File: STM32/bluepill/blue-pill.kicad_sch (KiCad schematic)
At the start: 36 parts, among them J1 USB_B_Micro, J2 J-Link, J3 BOOTx, J4 P3 Header, J5 P4 Header, SW1 RST, U1 RT9193, U2 STM32F103C8T6, Y1 8MHz, Y2 32.768k

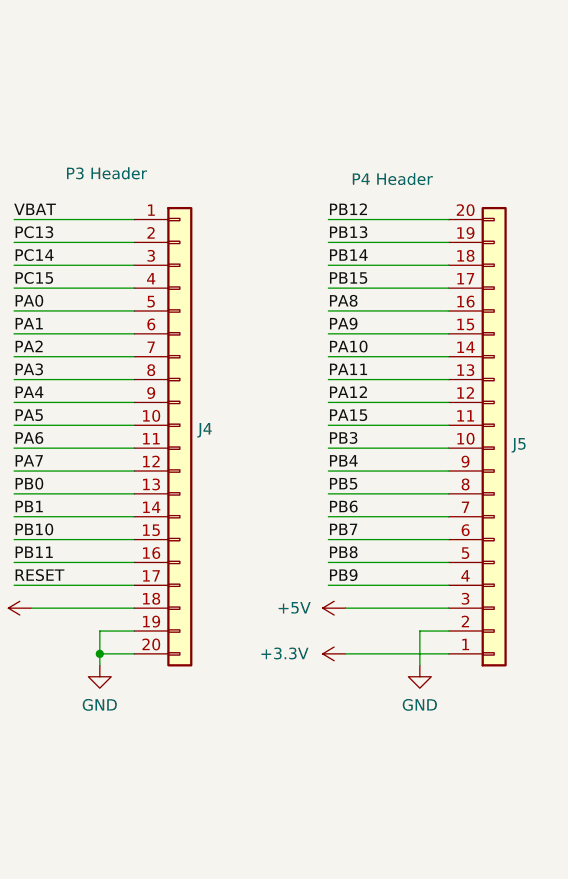
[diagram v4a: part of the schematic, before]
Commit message: Fix confusing P4 orientation
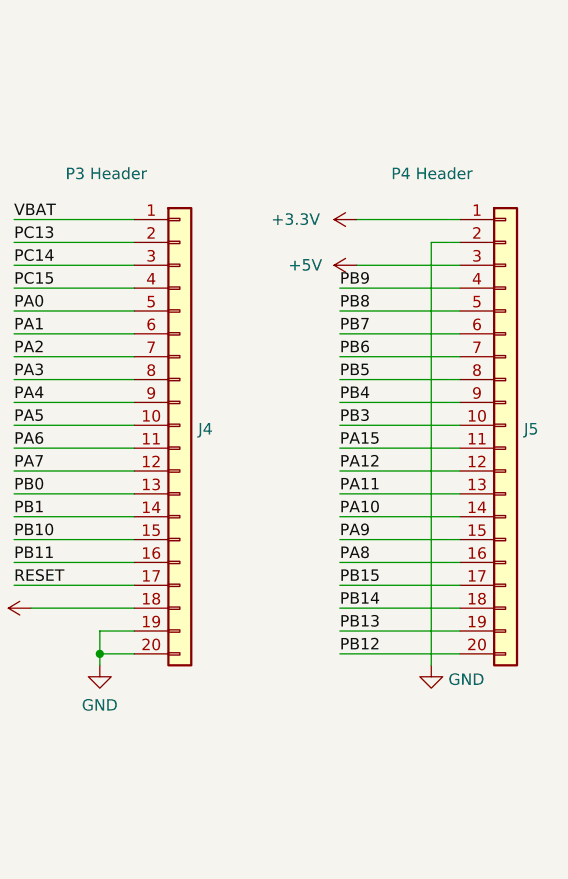
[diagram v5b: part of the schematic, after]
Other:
- moved on the sheet: J5

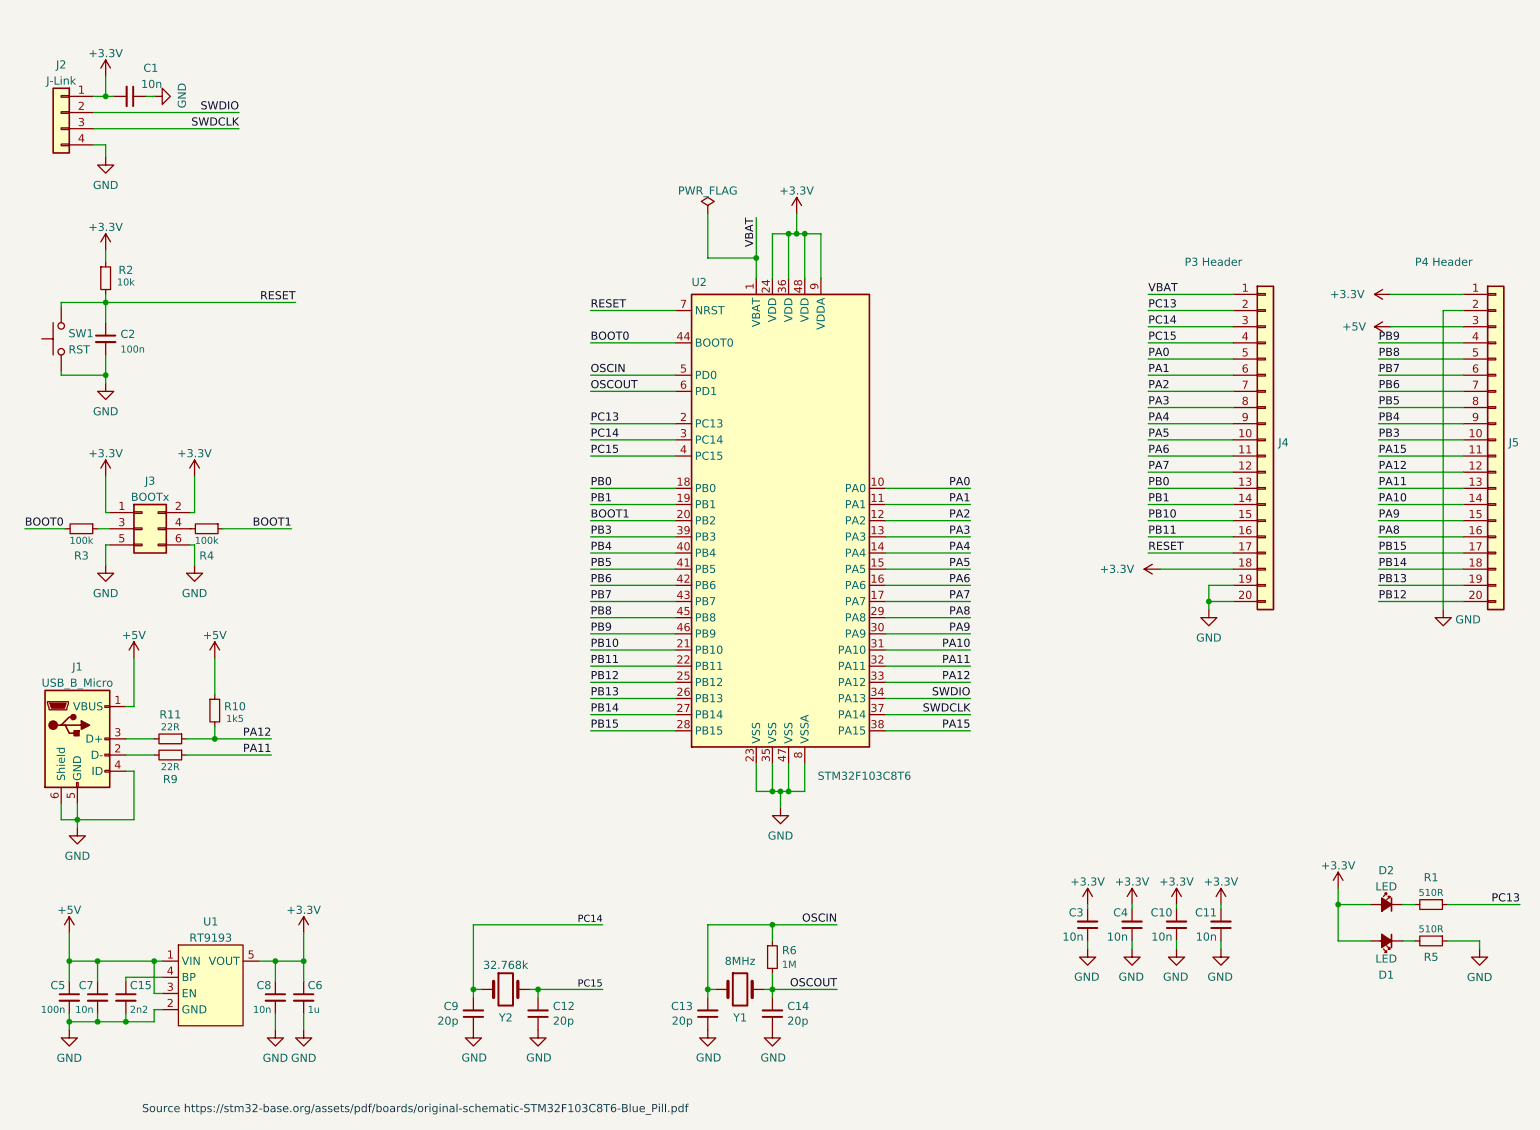
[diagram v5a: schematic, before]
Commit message: Fix grid alignment and update to KiCad 9
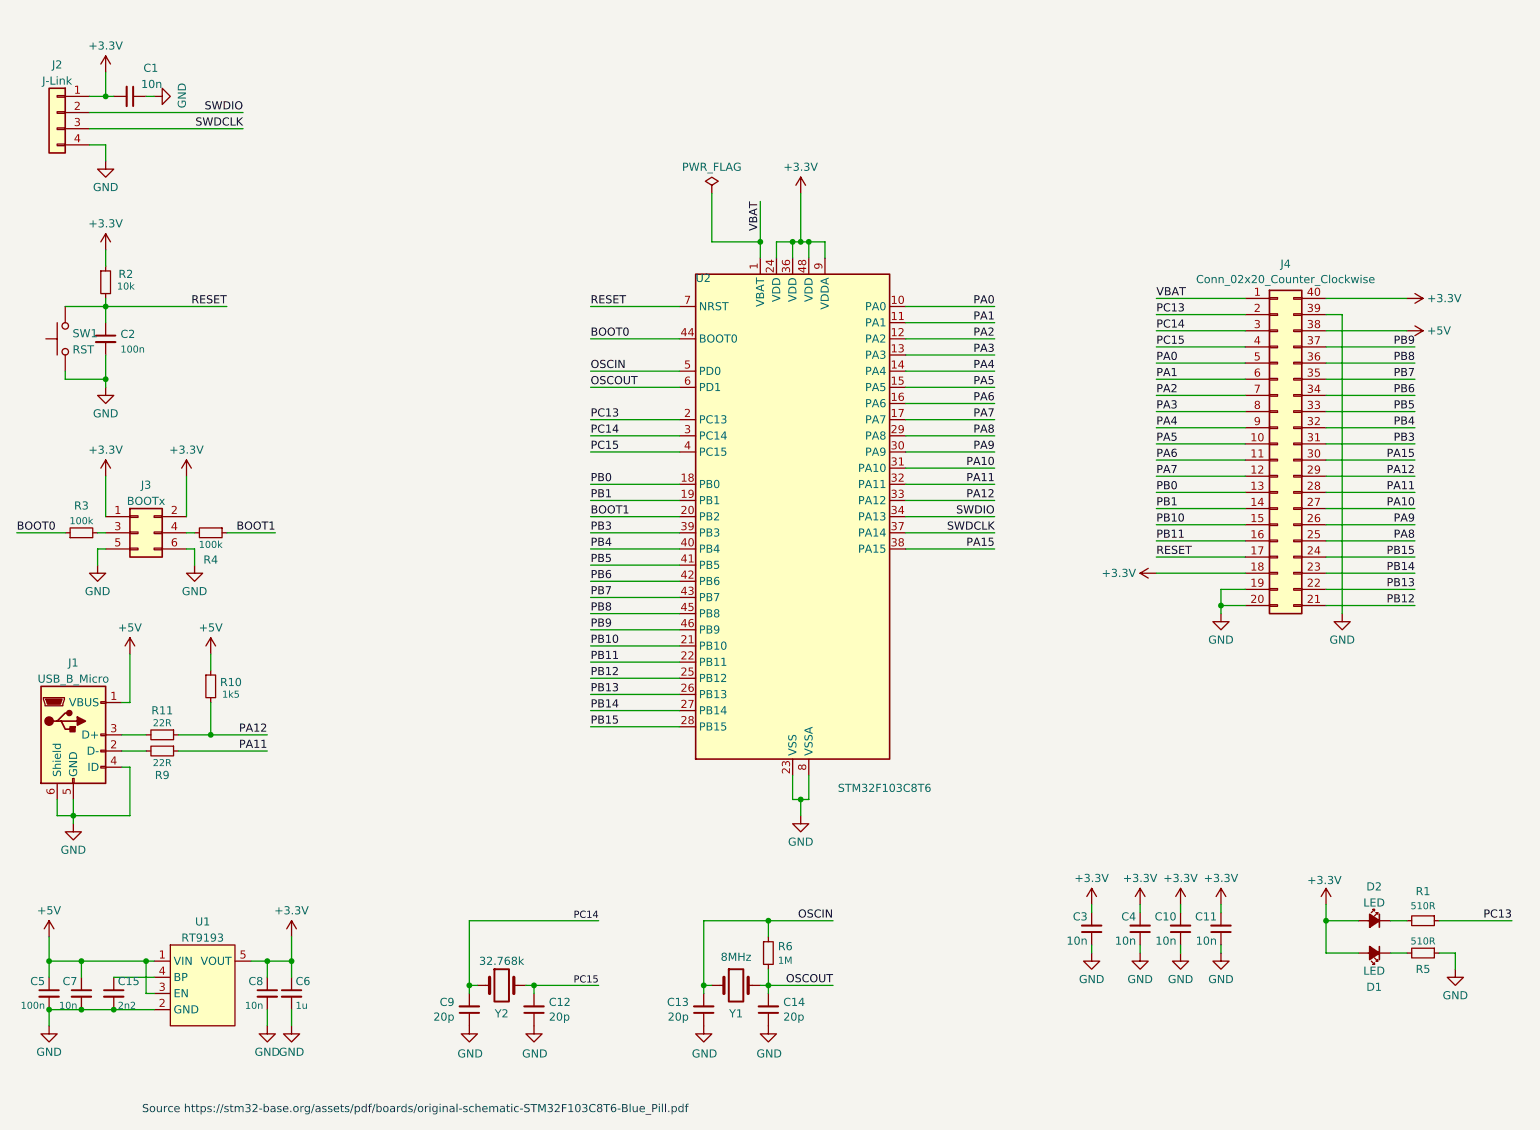
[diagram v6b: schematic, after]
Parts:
- removed J4: P3 Header, symbol Connector_Generic:Conn_01x20
- removed J5: P4 Header, symbol Connector_Generic:Conn_01x20
- added J4: Conn_02x20_Counter_Clockwise, symbol Connector_Generic:Conn_02x20_Counter_Clockwise
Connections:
- net +3.3V: now also J4.18 (Pin_18), J4.40 (Pin_40)
- net +5V: now also J4.38 (Pin_38)
- net BOOT0: now also R3.1; no longer R3.2
- net GND: now also J4.19 (Pin_19), J4.20 (Pin_20), J4.39 (Pin_39)
- net PA0: now also J4.5 (Pin_5)
- net PA1: now also J4.6 (Pin_6)
- net PA10: now also J4.27 (Pin_27)
- net PA11: now also J4.28 (Pin_28)
- net PA12: now also J4.29 (Pin_29)
- net PA15: now also J4.30 (Pin_30)
- net PA2: now also J4.7 (Pin_7)
- net PA3: now also J4.8 (Pin_8)
- net PA4: now also J4.9 (Pin_9)
- net PA5: now also J4.10 (Pin_10)
- net PA6: now also J4.11 (Pin_11)
- net PA7: now also J4.12 (Pin_12)
- net PA8: now also J4.25 (Pin_25)
- net PA9: now also J4.26 (Pin_26)
- net PB0: now also J4.13 (Pin_13)
- net PB1: now also J4.14 (Pin_14)
- net PB10: now also J4.15 (Pin_15)
- net PB11: now also J4.16 (Pin_16)
- net PB12: now also J4.21 (Pin_21)
- net PB13: now also J4.22 (Pin_22)
- net PB14: now also J4.23 (Pin_23)
- net PB15: now also J4.24 (Pin_24)
- net PB3: now also J4.31 (Pin_31)
- net PB4: now also J4.32 (Pin_32)
- net PB5: now also J4.33 (Pin_33)
- net PB6: now also J4.34 (Pin_34)
- net PB7: now also J4.35 (Pin_35)
- net PB8: now also J4.36 (Pin_36)
- net PB9: now also J4.37 (Pin_37)
- net PC13: now also J4.2 (Pin_2)
- net PC14: now also J4.3 (Pin_3)
- net PC15: now also J4.4 (Pin_4)
- net RESET: now also J4.17 (Pin_17)
- net VBAT: now also J4.1 (Pin_1)
- net at J3.3 (Pin_3): now also R3.2; no longer R3.1
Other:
- moved on the sheet: C10, C11, C12, C13, C14, C15, C3, C4, C5, C6, C7, C8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
